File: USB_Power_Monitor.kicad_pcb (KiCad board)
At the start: 4 copper layers, 46.1 x 21 mm, 55 parts, among them IC1 MCS1826GQTE-05-P, J1 USB_C_Receptacle, J2 USB_C_Plug, J5 Conn_01x01, J6 Conn_01x01, U1 RP2040, U2 L7983PU33R, U3 W25Q16JVSS, U4 TS3USB221AQRSERQ1, Y1 ABM8-272-T3

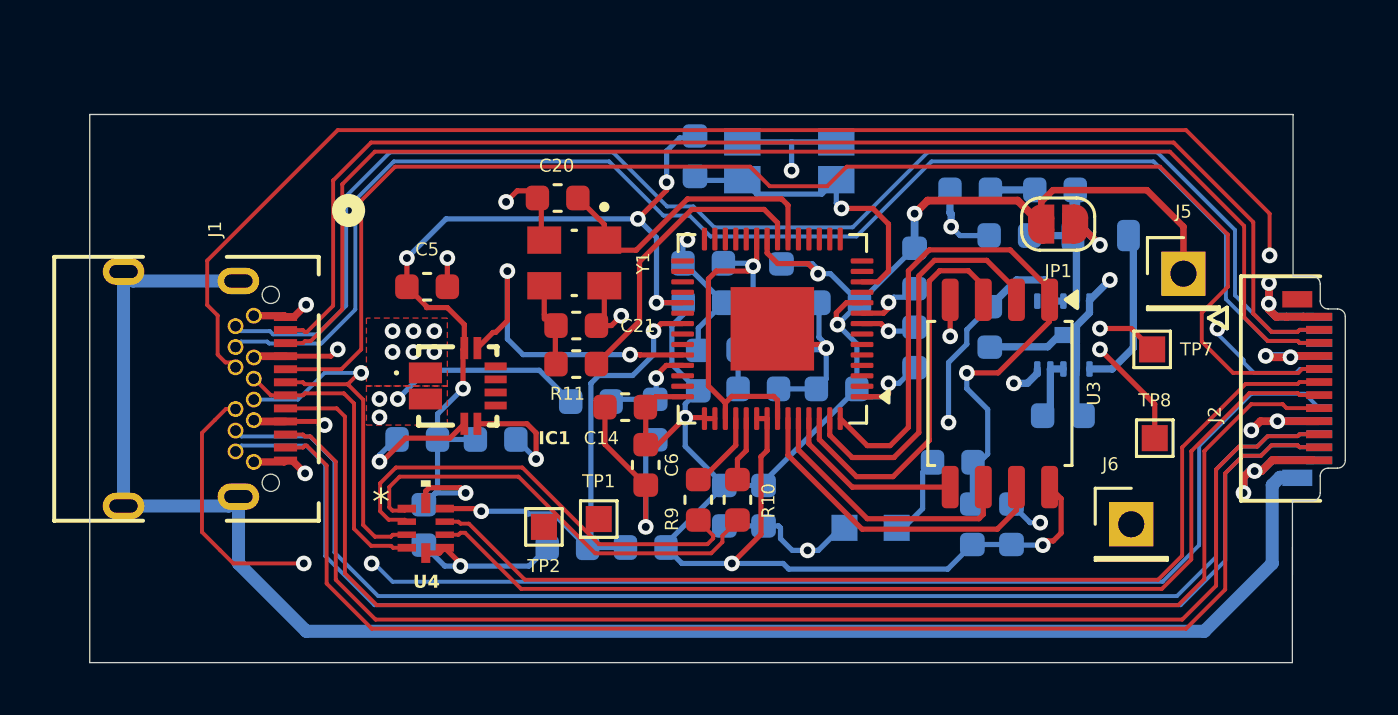
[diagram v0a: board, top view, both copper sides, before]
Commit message: Added SWD test points, roughly length matched qspi
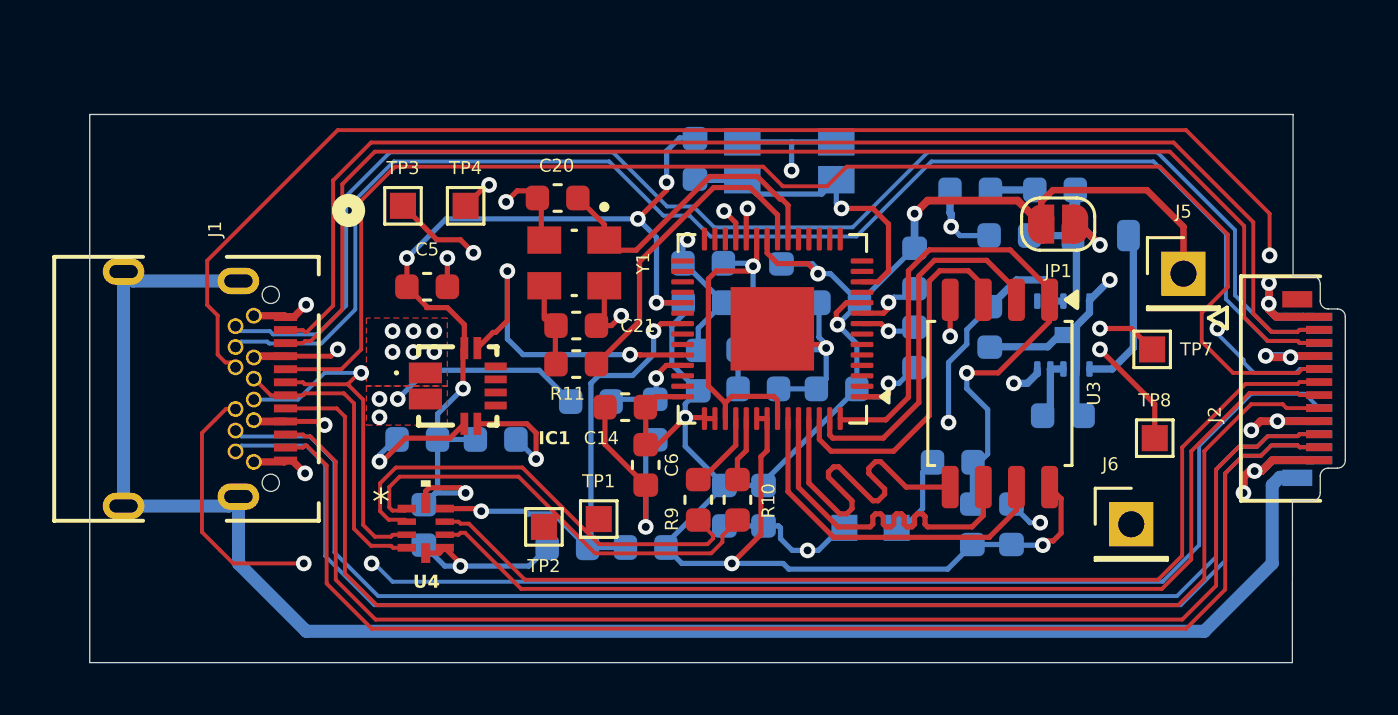
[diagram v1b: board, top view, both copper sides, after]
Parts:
- added TP3: TestPoint, TestPoint:TestPoint_Pad_1.0x1.0mm, F.Cu at (139.0, 91.0)
- added TP4: TestPoint, TestPoint:TestPoint_Pad_1.0x1.0mm, F.Cu at (141.4, 91.0)
- moved R5 0.10 mm to (150.2, 89.2)
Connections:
- U1 pad 24: unconnected-(U1-SWCLK-Pad24) -> Net-(U1-SWCLK)
- U1 pad 25: unconnected-(U1-SWDIO-Pad25) -> Net-(U1-SWDIO)
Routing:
- net Net-(U1-SWCLK): track 0.00 -> 16.2 mm, vias 0 -> 2
- net Net-(U1-SWDIO): track 0.00 -> 11.9 mm, vias 0 -> 2
- net /QSPI_SD0: track 7.07 -> 14.2 mm
- net /QSPI_SCLK: track 10.5 -> 13.9 mm
- net /QSPI_SS: track 26.7 -> 25.2 mm
- net /QSPI_SD2: track 15.3 -> 13.9 mm
- net /QSPI_SD1: track 15.6 -> 14.3 mm
- net /QSPI_SD3: track 12.5 -> 13.6 mm
- net /XOUT: track 11.6 -> 12.4 mm
- net /XIN: track 11.4 -> 12.2 mm

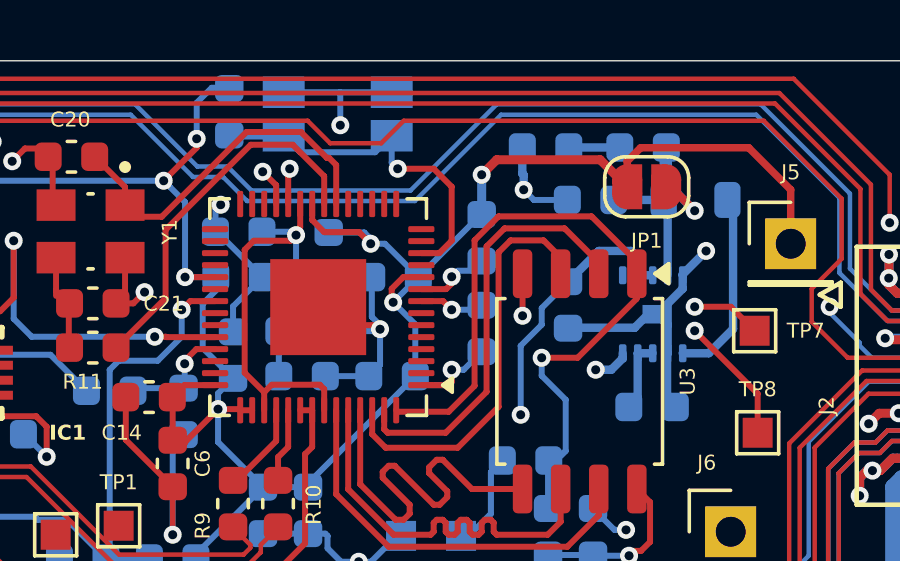
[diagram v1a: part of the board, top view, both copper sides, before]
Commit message: Increase 3.3V trace width, add teardrops, generate fab files
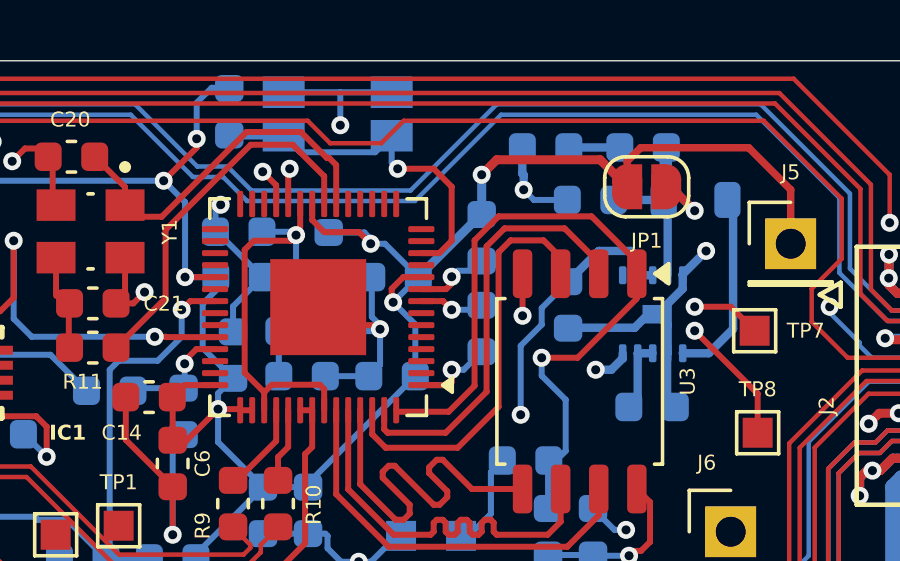
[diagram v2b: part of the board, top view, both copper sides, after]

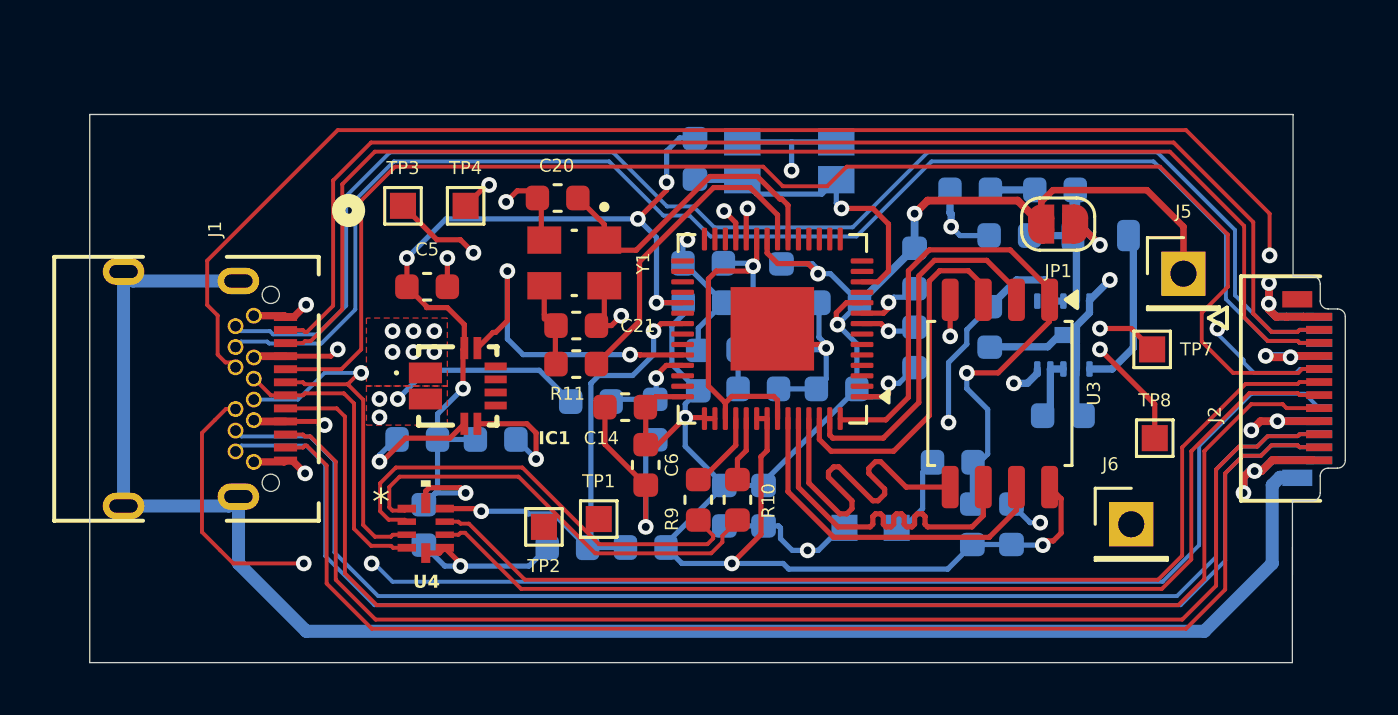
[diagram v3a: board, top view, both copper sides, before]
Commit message: Fixed GND plane, add mounting holes
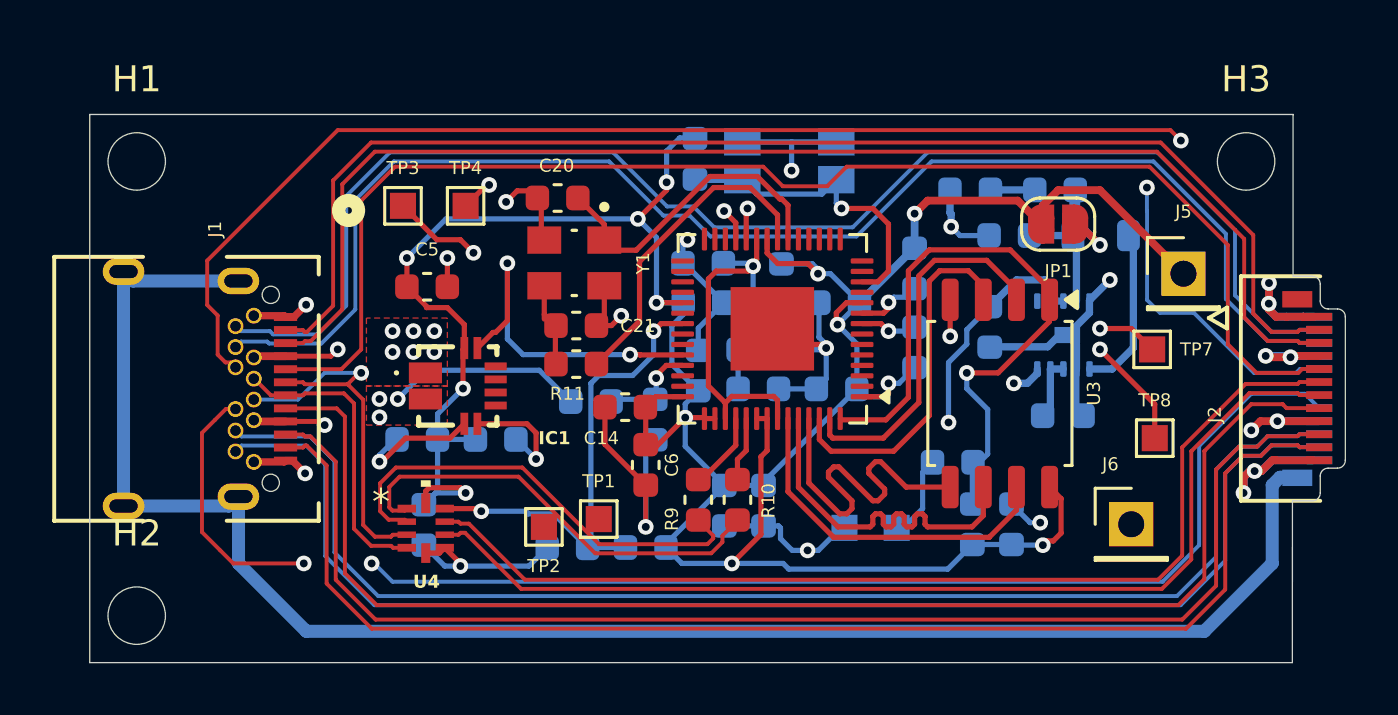
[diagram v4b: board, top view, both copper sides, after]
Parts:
- added H1: MountingHole, MountingHole:MountingHole_2.2mm_M2, F.Cu at (128.8, 89.3)
- added H2: MountingHole, MountingHole:MountingHole_2.2mm_M2, F.Cu at (128.8, 106.7)
- added H3: MountingHole, MountingHole:MountingHole_2.2mm_M2, F.Cu at (171.3, 89.3)
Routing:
- net /CC1: track 53.9 -> 52.3 mm
- net +3.3V: track 120.5 -> 119.3 mm
- net /Vcurr: track 13.1 -> 13.7 mm
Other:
- rule pad_to_mask_clearance: 0 -> 0.05
- board text added: "0"
- board text added: "0 mm"
- board text added: "0.01 mm"
- board text added: "0.02"
- board text added: "0.035 mm"
- board text added: "0.092 mm"
- board text added: "0.1000 mm / 0.1000 mm"
- board text added: "0.1500 mm"
- board text added: "0.5 mm"
- board text added: "0.8440 mm"
- board text added: "1"
- board text added: "3.3"
- board text added: "4"
- board text added: "4.74"
- board text added: "48.1000 mm x 21.0000 mm"
- board text added: "B.Cu"
- board text added: "B.Mask"
- board text added: "B.Paste"
- board text added: "B.Silkscreen"
- board text added: "BOARD CHARACTERISTICS"
- board text added: "Board Thickness:"
- board text added: "Board overall dimensions:"
- board text added: "Bottom Silk Screen"
- board text added: "Bottom Solder Mask"
- board text added: "Bottom Solder Paste"
- board text added: "Castellated pads:"
- board text added: "Color"
- board text added: "Copper Finish:"
- board text added: "Copper Layer Count:"
- board text added: "Dielectric 1"
- board text added: "Dielectric 2"
- board text added: "Dielectric 3"
- board text added: "Edge card connectors:"
- board text added: "Epsilon R"
- board text added: "F.Cu"
- board text added: "F.Mask"
- board text added: "F.Paste"
- board text added: "F.Silkscreen"
- board text added: "FR4"
- board text added: "Impedance Control:"
- board text added: "In1.Cu"
- board text added: "In2.Cu"
- board text added: "Layer Name"
- board text added: "Loss Tangent"
- board text added: "Material"
- board text added: "Min hole diameter:"
- board text added: "Min track/spacing:"
- board text added: "No"
- board text added: "None"
- board text added: "Not specified"
- board text added: "Plated Board Edge:"
- board text added: "Thickness (mm)"
- board text added: "Top Silk Screen"
- board text added: "Top Solder Mask"
- board text added: "Top Solder Paste"
- board text added: "Type"
- board text added: "Yes"
- board text added: "copper"
- board text added: "core"
- board text added: "prepreg"
